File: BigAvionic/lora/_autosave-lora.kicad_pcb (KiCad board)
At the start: 2 copper layers, 68 x 68 mm, 14 parts, among them U10 E22-400T30S, U11 E80-900M23313S

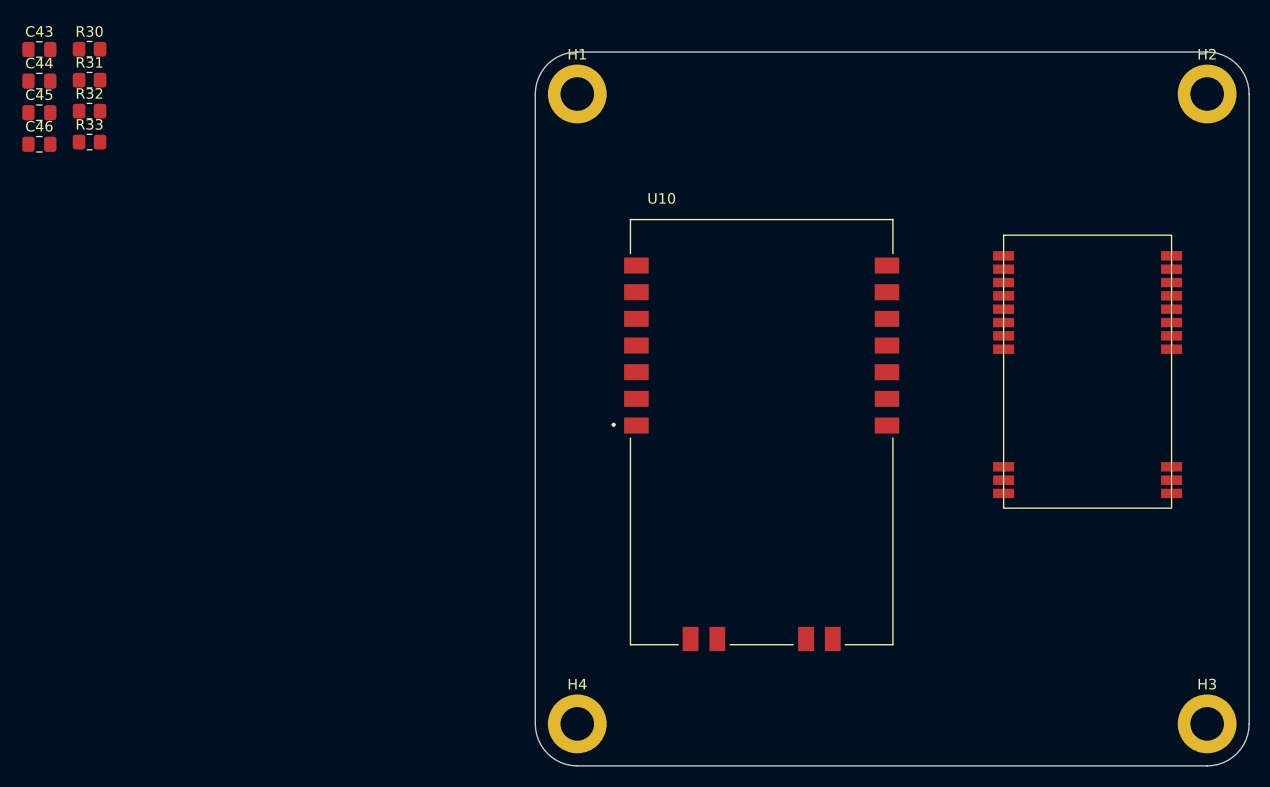
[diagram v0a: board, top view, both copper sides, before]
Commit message: add new power layer
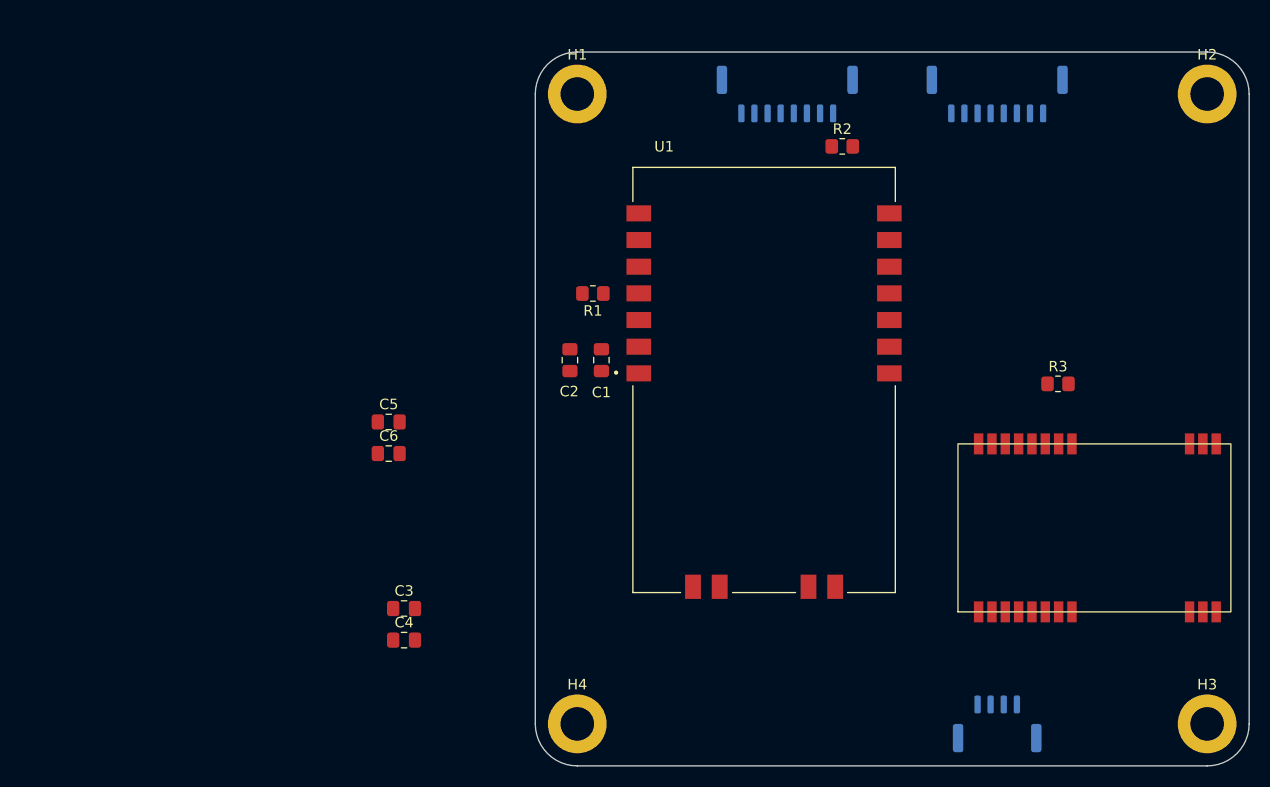
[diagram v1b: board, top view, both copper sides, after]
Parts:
- removed R30: 22ohm, Resistor_SMD:R_0805_2012Metric_Pad1.20x1.40mm_HandSolder
- added C5: 100n, Capacitor_SMD:C_0805_2012Metric_Pad1.18x1.45mm_HandSolder, F.Cu at (105.3, 92.4)
- added C6: 100n, Capacitor_SMD:C_0805_2012Metric_Pad1.18x1.45mm_HandSolder, F.Cu at (105.3, 95.5)
- added J1: Conn_01x04, Connector_JST:JST_GH_SM04B-GHS-TB_1x04-1MP_P1.25mm_Horizontal, B.Cu at (163.2, 121.2)
- added J2: Conn_01x08, Connector_JST:JST_GH_SM08B-GHS-TB_1x08-1MP_P1.25mm_Horizontal, B.Cu at (143.2, 61.2)
- added J3: Conn_01x08, Connector_JST:JST_GH_SM08B-GHS-TB_1x08-1MP_P1.25mm_Horizontal, B.Cu at (163.2, 61.2)
- moved R3 95.1 mm to (169.0, 88.8)
- moved R2 71.8 mm to (148.5, 66.2)
- moved C1 61.2 mm to (125.5, 86.5), turned to -90 degrees
- moved C3 58.6 mm to (106.7, 110.2)
- moved C4 58.6 mm to (106.7, 113.2)
- moved C2 57.1 mm to (122.5, 86.5), turned to -90 degrees
- moved R1 52.1 mm to (124.7, 80.2), turned to 180 degrees
- moved U2 14.9 mm to (172.5, 102.5), turned to 90 degrees
- moved U1 4.98 mm to (141.0, 88.4)
- renumbered C43 to C1, C44 to C2, C45 to C3, C46 to C4, R31 to R1, R32 to R2, R33 to R3, U10 to U1, U11 to U2
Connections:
- U1 pad 5: Net-(U10-RXD) -> UART3_TX
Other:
- copper layers 2 -> 4
